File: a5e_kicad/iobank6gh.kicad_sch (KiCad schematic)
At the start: 5 parts, among them U1 A5EB013B-B23B, U901 M41T62LC6F

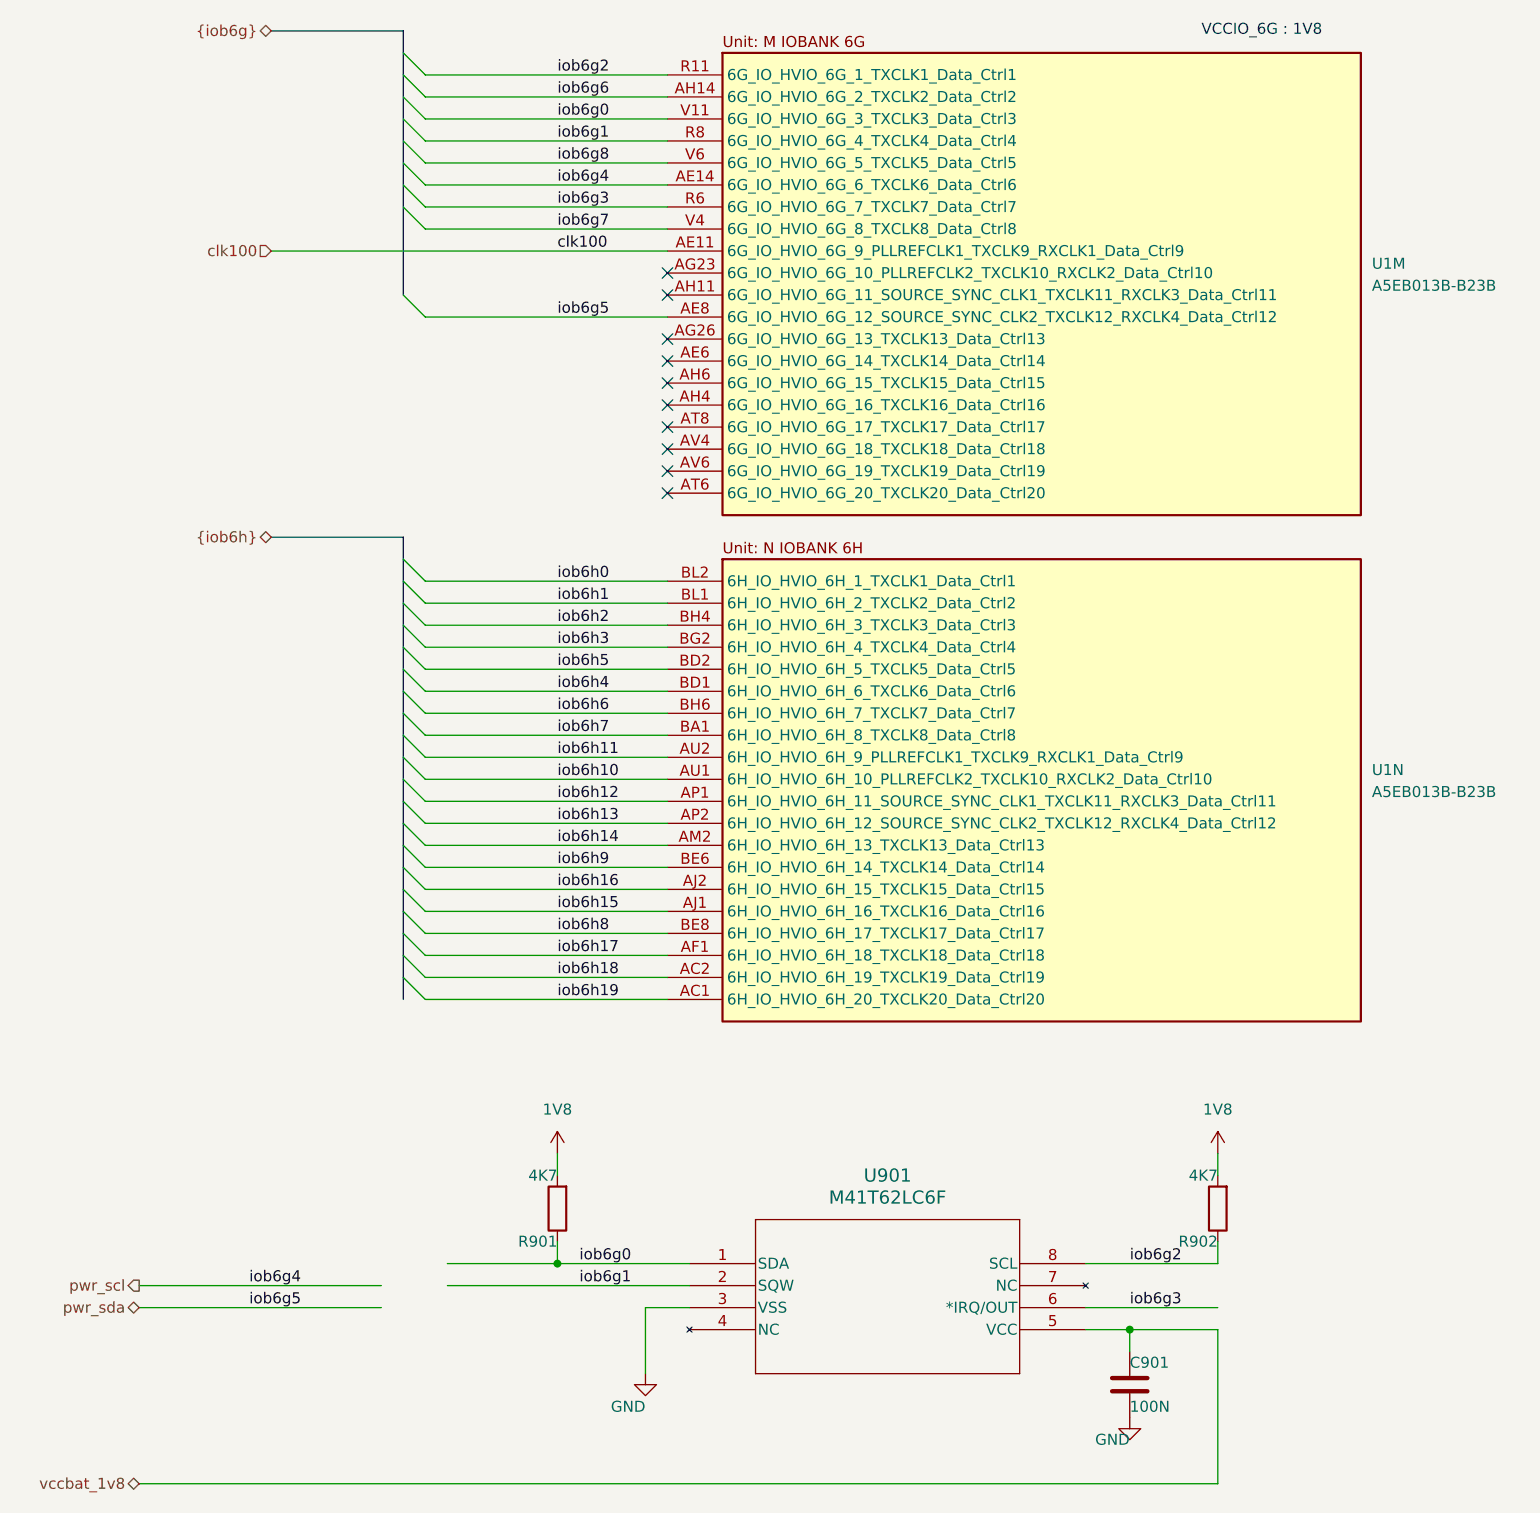
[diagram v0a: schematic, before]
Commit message: add vias to lppdr balls
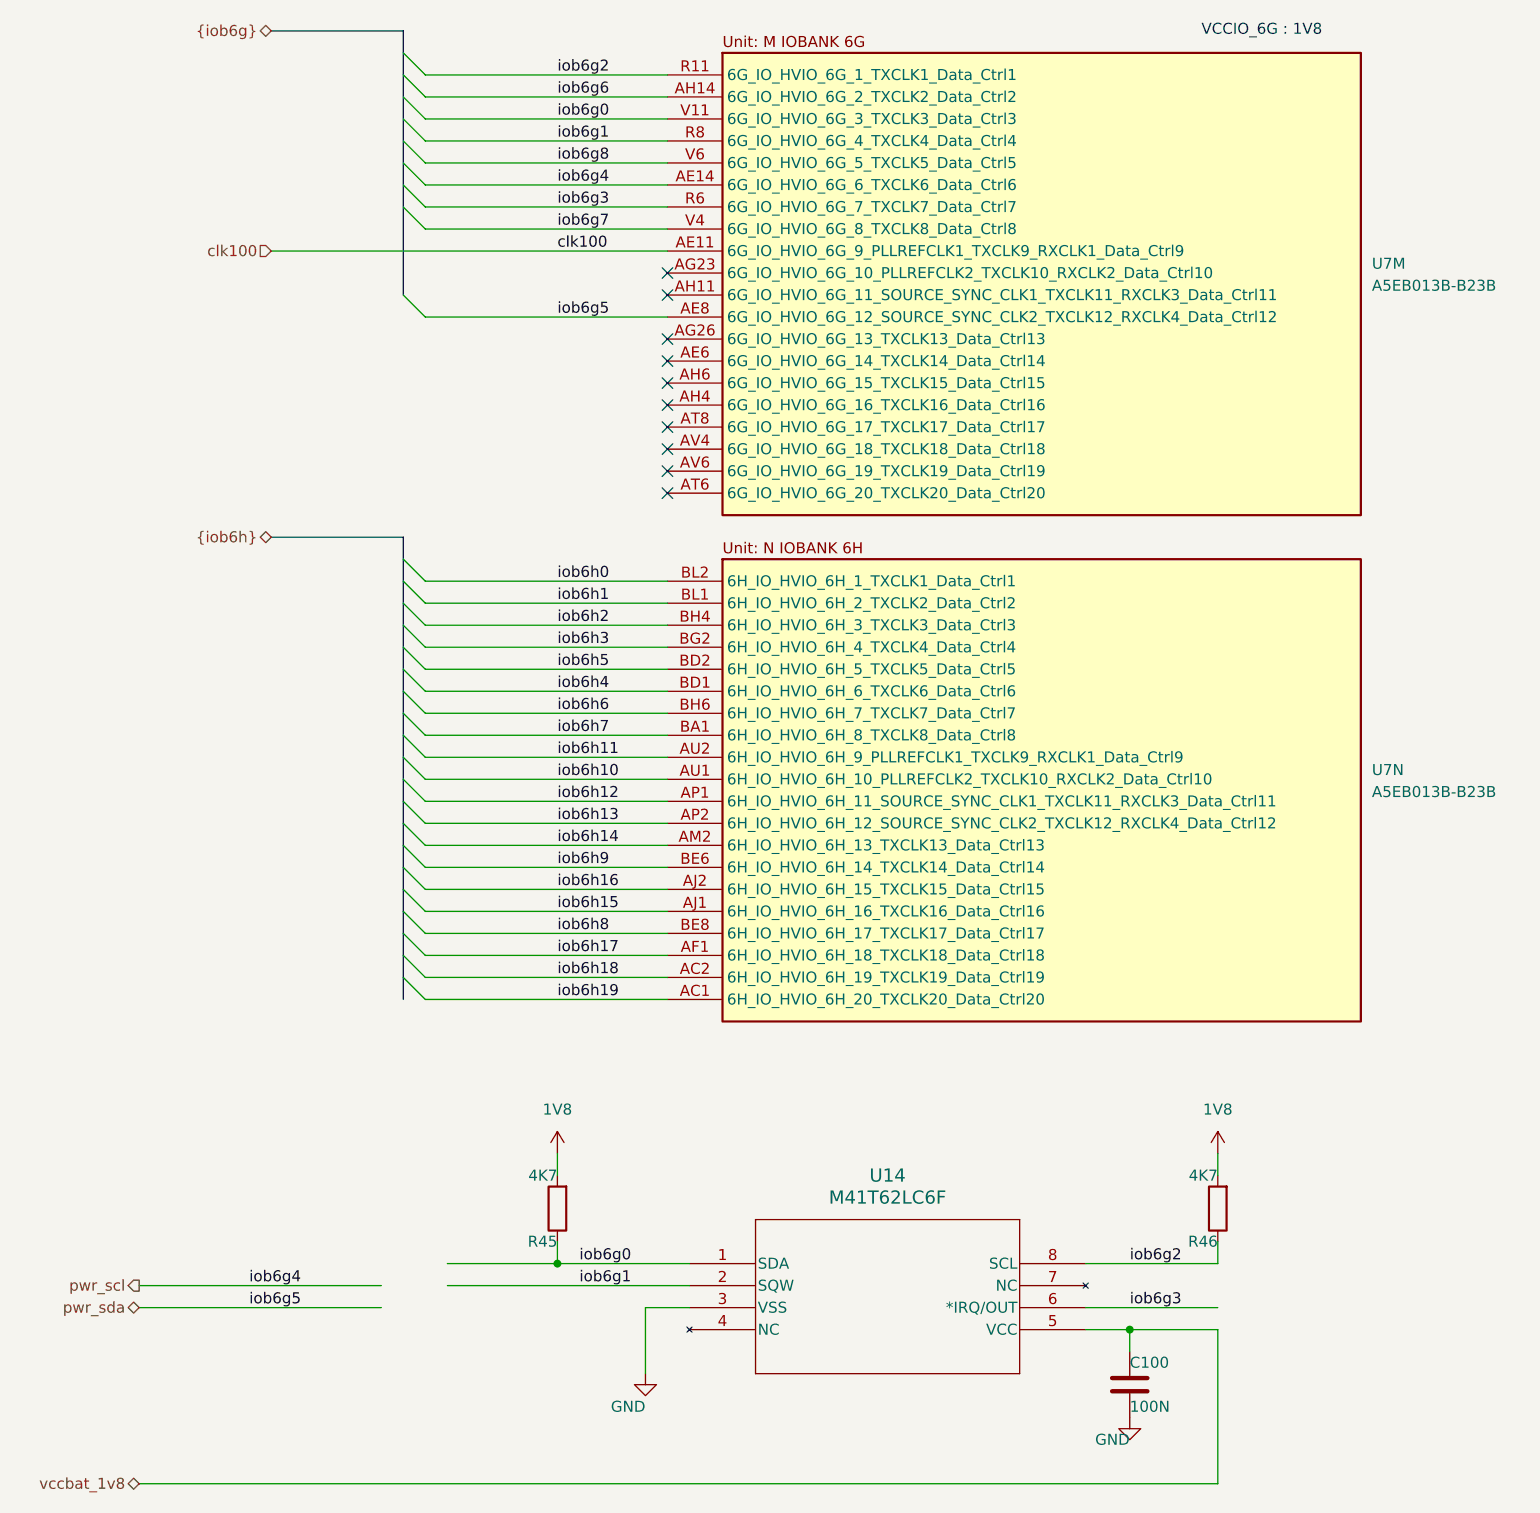
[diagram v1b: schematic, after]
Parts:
- renumbered C901 to C100, R901 to R45, R902 to R46, U901 to U14, U1 to U7
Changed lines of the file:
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@@
 		(in_pos_files yes)
 		(dnp no)
-		(property "Reference" "R901"
+		(property "Reference" "R45"
 			(at 83.82 162.56 0)
 			(show_name no)
@@
 			(project "agilex_3_soc"
 				(path "/a5b98d95-6877-4284-904f-d04e32723ae0/daebef0d-cd15-4e03-815a-780dc10d7764"
-					(reference "R901")
+					(reference "R45")
 					(unit 1)
 				)
@@
 		(in_pos_files yes)
 		(dnp no)
-		(property "Reference" "C901"
+		(property "Reference" "C100"
 			(at 149.86 176.53 0)
 			(show_name no)
@@
 			(project "agilex_3_soc"
 				(path "/a5b98d95-6877-4284-904f-d04e32723ae0/daebef0d-cd15-4e03-815a-780dc10d7764"
-					(reference "C901")
+					(reference "C100")
 					(unit 1)
 				)
@@
 		(dnp no)
 		(fields_autoplaced yes)
-		(property "Reference" "#PWR0906"
+		(property "Reference" "#PWR0182"
 			(at 83.82 156.21 0)
 			(hide yes)
@@
 			(project "agilex_3_soc"
 				(path "/a5b98d95-6877-4284-904f-d04e32723ae0/daebef0d-cd15-4e03-815a-780dc10d7764"
-					(reference "#PWR0906")
+					(reference "#PWR0182")
 					(unit 1)
 				)
@@
 		(dnp no)
 		(fields_autoplaced yes)
-		(property "Reference" "U1"
+		(property "Reference" "U7"
 			(at 177.8 108.1376 0)
 			(show_name no)
@@
 			(project "agilex_3_soc"
 				(path "/a5b98d95-6877-4284-904f-d04e32723ae0/daebef0d-cd15-4e03-815a-780dc10d7764"
-					(reference "U1")
+					(reference "U7")
 					(unit 14)
 				)
@@
 		(in_pos_files yes)
 		(dnp no)
-		(property "Reference" "R902"
+		(property "Reference" "R46"
 			(at 160.02 162.56 0)
 			(show_name no)
@@
 			(project "agilex_3_soc"
 				(path "/a5b98d95-6877-4284-904f-d04e32723ae0/daebef0d-cd15-4e03-815a-780dc10d7764"
-					(reference "R902")
+					(reference "R46")
 					(unit 1)
 				)
@@
 		(dnp no)
 		(fields_autoplaced yes)
-		(property "Reference" "#PWR0909"
+		(property "Reference" "#PWR0185"
 			(at 160.02 156.21 0)
 			(hide yes)
@@
 			(project "agilex_3_soc"
 				(path "/a5b98d95-6877-4284-904f-d04e32723ae0/daebef0d-cd15-4e03-815a-780dc10d7764"
-					(reference "#PWR0909")
+					(reference "#PWR0185")
 					(unit 1)
 				)
@@
 		(dnp no)
 		(fields_autoplaced yes)
-		(property "Reference" "U901"
+		(property "Reference" "U14"
 			(at 121.92 154.94 0)
 			(show_name no)
@@
 			(project "agilex_3_soc"
 				(path "/a5b98d95-6877-4284-904f-d04e32723ae0/daebef0d-cd15-4e03-815a-780dc10d7764"
-					(reference "U901")
+					(reference "U14")
 					(unit 1)
 				)
@@
 		(in_pos_files yes)
 		(dnp no)
-		(property "Reference" "#PWR0908"
+		(property "Reference" "#PWR0184"
 			(at 149.86 189.23 0)
 			(hide yes)
@@
 			(project "agilex_3_soc"
 				(path "/a5b98d95-6877-4284-904f-d04e32723ae0/daebef0d-cd15-4e03-815a-780dc10d7764"
-					(reference "#PWR0908")
+					(reference "#PWR0184")
 					(unit 1)
 				)
@@
 		(dnp no)
 		(fields_autoplaced yes)
-		(property "Reference" "U1"
+		(property "Reference" "U7"
 			(at 177.8 49.7176 0)
 			(show_name no)
@@
 			(project "agilex_3_soc"
 				(path "/a5b98d95-6877-4284-904f-d04e32723ae0/daebef0d-cd15-4e03-815a-780dc10d7764"
-					(reference "U1")
+					(reference "U7")
 					(unit 13)
 				)
@@
 		(in_pos_files yes)
 		(dnp no)
-		(property "Reference" "#PWR0907"
+		(property "Reference" "#PWR0183"
 			(at 93.98 184.15 0)
 			(hide yes)
@@
 			(project "agilex_3_soc"
 				(path "/a5b98d95-6877-4284-904f-d04e32723ae0/daebef0d-cd15-4e03-815a-780dc10d7764"
-					(reference "#PWR0907")
+					(reference "#PWR0183")
 					(unit 1)
 				)

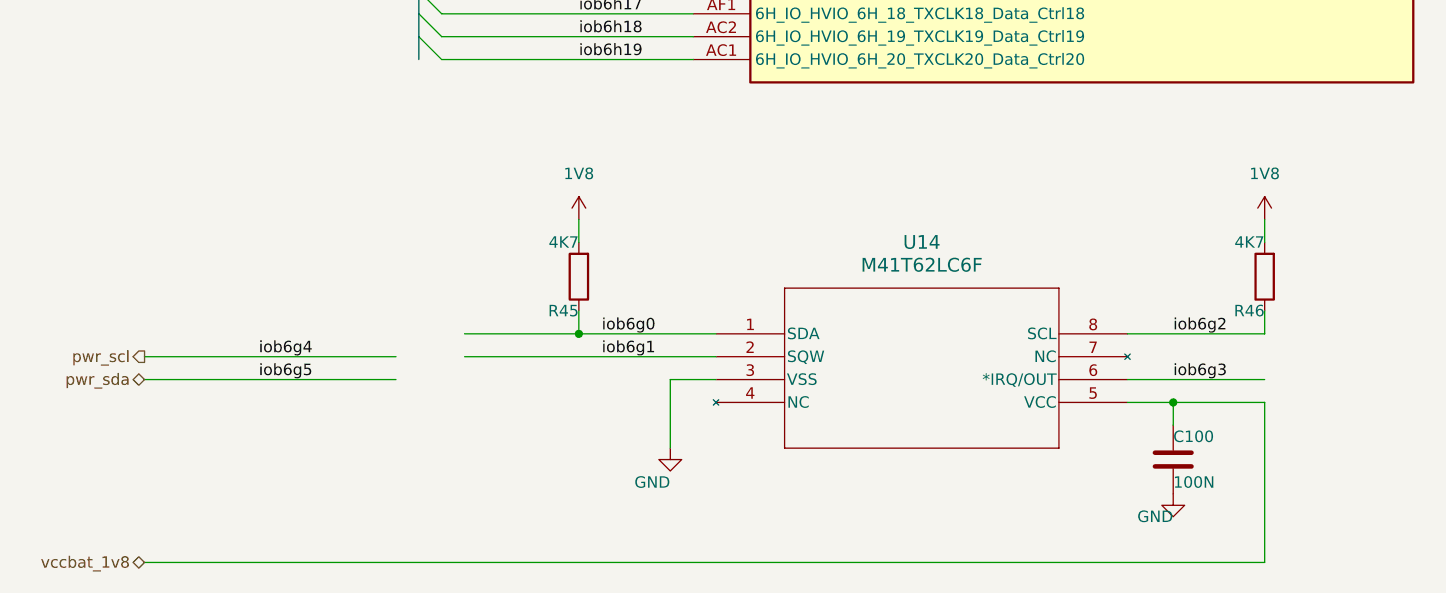
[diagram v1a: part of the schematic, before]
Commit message: remove hyperram and add lpddr4 bypass caps
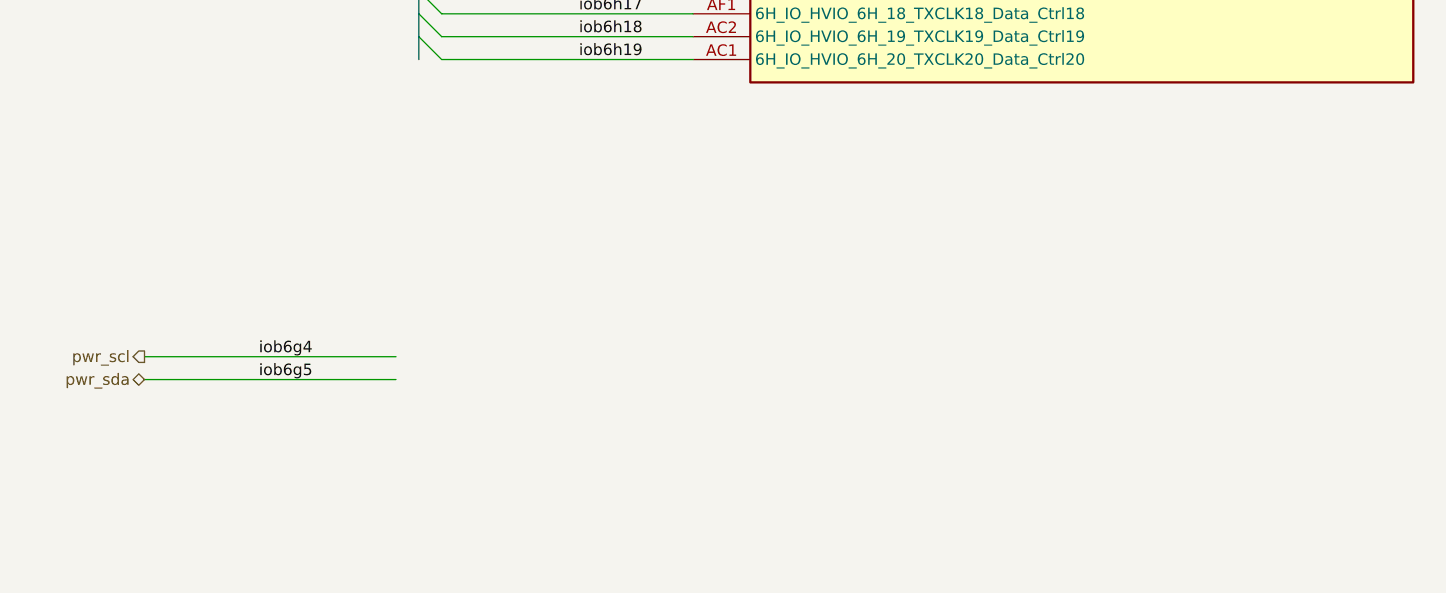
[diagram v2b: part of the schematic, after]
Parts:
- removed C100: 100N, Capacitor_SMD:C_0402_1005Metric, symbol Device:C
- removed R45, R46: 4K7, Resistor_SMD:R_0402_1005Metric, symbol Device:R
- removed U14: M41T62LC6F, symbol M41T62LC:M41T62LC6F
